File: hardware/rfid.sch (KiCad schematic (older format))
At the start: 29 parts

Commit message: Annotated schematic, generated netlist, and assigned footprints to all of the passives. Only connectors, IC, and crystal footprints have to be made and assigned.
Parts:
- gave numbers to parts that had none: 29
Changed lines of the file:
@@
 $EndDescr
 $Comp
-L CR95HF U?
+L CR95HF U1
 U 1 1 541504F3
 P 3525 2245
-F 0 "U?" H 3990 3230 39  0000 C CNN
+F 0 "U1" H 3990 3230 39  0000 C CNN
 F 1 "CR95HF" H 3015 3230 39  0000 C CNN
 F 2 "" H 3485 2765 20  0000 C CNN
@@
 $EndComp
 $Comp
-L MURATA_CRYSTAL_SMD X?
+L MURATA_CRYSTAL_SMD X1
 U 1 1 54173929
 P 2365 2700
-F 0 "X?" V 2255 2765 30  0000 C CNN
+F 0 "X1" V 2255 2765 30  0000 C CNN
 F 1 "27.12MHz" V 2370 2770 30  0000 L CNN
 F 2 "" H 2365 2700 60  0000 C CNN
@@
 $EndComp
 $Comp
-L capacitor C?
+L capacitor C1
 U 1 1 54173C81
 P 2020 2530
-F 0 "C?" V 1980 2585 40  0000 L CNN
+F 0 "C1" V 1980 2585 40  0000 L CNN
 F 1 "4pF" V 1970 2370 40  0000 L CNN
 F 2 "" H 2058 2380 30  0000 C CNN
@@
 $EndComp
 $Comp
-L capacitor C?
+L capacitor C2
 U 1 1 54173DFA
 P 2020 2870
-F 0 "C?" V 1975 2920 40  0000 L CNN
+F 0 "C2" V 1975 2920 40  0000 L CNN
 F 1 "4pF" V 1965 2710 40  0000 L CNN
 F 2 "" H 2058 2720 30  0000 C CNN
@@
 Connection ~ 2365 2870
 $Comp
-L GND #PWR?
+L GND #PWR01
 U 1 1 54173FD6
 P 1670 2730
-F 0 "#PWR?" H 1670 2730 30  0001 C CNN
+F 0 "#PWR01" H 1670 2730 30  0001 C CNN
 F 1 "GND" H 1670 2660 30  0001 C CNN
 F 2 "" H 1670 2730 60  0000 C CNN
@@
 Connection ~ 1800 2660
 $Comp
-L capacitor C?
+L capacitor C7
 U 1 1 54175E86
 P 2690 3385
-F 0 "C?" H 2710 3460 40  0000 L CNN
+F 0 "C7" H 2710 3460 40  0000 L CNN
 F 1 "1nF" H 2710 3305 40  0000 L CNN
 F 2 "" H 2728 3235 30  0000 C CNN
@@
 	2690 3180 2690 3275
 $Comp
-L GND #PWR?
+L GND #PWR02
 U 1 1 54175FA9
 P 2690 3545
-F 0 "#PWR?" H 2690 3545 30  0001 C CNN
+F 0 "#PWR02" H 2690 3545 30  0001 C CNN
 F 1 "GND" H 2690 3475 30  0001 C CNN
 F 2 "" H 2690 3545 60  0000 C CNN
@@
 3V3
 $Comp
-L resistor R?
+L resistor R4
 U 1 1 54191892
 P 2635 1310
-F 0 "R?" H 2550 1360 40  0000 C CNN
+F 0 "R4" H 2550 1360 40  0000 C CNN
 F 1 "3.3k" H 2560 1440 40  0000 C CNN
 F 2 "" V 2565 1310 30  0000 C CNN
@@
 Connection ~ 3495 1100
 $Comp
-L GND #PWR?
+L GND #PWR03
 U 1 1 54191BE5
 P 2680 2355
-F 0 "#PWR?" H 2680 2355 30  0001 C CNN
+F 0 "#PWR03" H 2680 2355 30  0001 C CNN
 F 1 "GND" H 2680 2285 30  0001 C CNN
 F 2 "" H 2680 2355 60  0000 C CNN
@@
 	2205 2065 2785 2065
 $Comp
-L CONN_01X06 P?
+L CONN_01X06 P2
 U 1 1 54192185
 P 2005 1815
-F 0 "P?" H 2005 1465 50  0000 C CNN
+F 0 "P2" H 2005 1465 50  0000 C CNN
 F 1 "COMMS" V 2105 1815 50  0000 C CNN
 F 2 "" H 2005 1815 60  0000 C CNN
@@
 	2300 1565 2205 1565
 $Comp
-L resistor R?
+L resistor R1
 U 1 1 541A2E55
 P 2425 1310
-F 0 "R?" H 2330 1360 40  0000 C CNN
+F 0 "R1" H 2330 1360 40  0000 C CNN
 F 1 "3.3k" H 2355 1440 40  0000 C CNN
 F 2 "" V 2355 1310 30  0000 C CNN
@@
 Connection ~ 2635 1100
 $Comp
-L resistor R?
+L resistor R2
 U 1 1 541A325E
 P 2450 2210
-F 0 "R?" V 2375 2285 40  0000 C CNN
+F 0 "R2" V 2375 2285 40  0000 C CNN
 F 1 "3.3k" V 2375 2135 40  0000 C CNN
 F 2 "" V 2380 2210 30  0000 C CNN
@@
 	2235 2210 2270 2210
 $Comp
-L resistor R?
+L resistor R3
 U 1 1 541A35D8
 P 2460 3100
-F 0 "R?" V 2375 3165 40  0000 C CNN
+F 0 "R3" V 2375 3165 40  0000 C CNN
 F 1 "3.3k" V 2375 3020 40  0000 C CNN
 F 2 "" V 2390 3100 30  0000 C CNN
@@
 	2185 3100 2280 3100
 $Comp
-L GND #PWR?
+L GND #PWR04
 U 1 1 541A40A6
 P 3525 3530
-F 0 "#PWR?" H 3525 3530 30  0001 C CNN
+F 0 "#PWR04" H 3525 3530 30  0001 C CNN
 F 1 "GND" H 3525 3460 30  0001 C CNN
 F 2 "" H 3525 3530 60  0000 C CNN
@@
 Connection ~ 3525 3475
 $Comp
-L CONN_01X02 P?
+L CONN_01X02 P1
 U 1 1 541A49C8
 P 1775 4235
-F 0 "P?" H 1775 4385 50  0000 C CNN
+F 0 "P1" H 1775 4385 50  0000 C CNN
 F 1 "CONN_01X02" V 1875 4235 50  0000 C CNN
 F 2 "" H 1775 4235 60  0000 C CNN
@@
 	3580 1175 3580 1050
 $Comp
-L GND #PWR?
+L GND #PWR05
 U 1 1 541A5357
 P 2030 4335
-F 0 "#PWR?" H 2030 4335 30  0001 C CNN
+F 0 "#PWR05" H 2030 4335 30  0001 C CNN
 F 1 "GND" H 2030 4265 30  0001 C CNN
 F 2 "" H 2030 4335 60  0000 C CNN
@@
 3V3_RF
 $Comp
-L INDUCTOR_SMALL L?
+L INDUCTOR_SMALL L1
 U 1 1 541A56A3
 P 2190 4515
-F 0 "L?" H 2190 4615 50  0000 C CNN
+F 0 "L1" H 2190 4615 50  0000 C CNN
 F 1 "tx_3v3_choke" H 2190 4465 50  0000 C CNN
 F 2 "" H 2190 4515 60  0000 C CNN
@@
 $EndComp
 $Comp
-L capacitor C?
+L capacitor C3
 U 1 1 541A58CF
 P 2425 4370
-F 0 "C?" H 2445 4445 40  0000 L CNN
+F 0 "C3" H 2445 4445 40  0000 L CNN
 F 1 "10nF" H 2440 4285 40  0000 L CNN
 F 2 "" H 2463 4220 30  0000 C CNN
@@
 $EndComp
 $Comp
-L capacitor C?
+L capacitor C5
 U 1 1 541A5A22
 P 2685 4370
-F 0 "C?" H 2705 4445 40  0000 L CNN
+F 0 "C5" H 2705 4445 40  0000 L CNN
 F 1 "100nF" H 2705 4280 40  0000 L CNN
 F 2 "" H 2723 4220 30  0000 C CNN
@@
 $EndComp
 $Comp
-L Polarized_Capacitor C?
+L Polarized_Capacitor C8
 U 1 1 541A5A83
 P 2965 4365
-F 0 "C?" H 2990 4440 39  0000 L CNN
+F 0 "C8" H 2990 4440 39  0000 L CNN
 F 1 "1uF" H 3015 4270 39  0000 L CNN
 F 2 "" H 2965 4365 60  0000 C CNN
@@
 $EndComp
 $Comp
-L Polarized_Capacitor C?
+L Polarized_Capacitor C9
 U 1 1 541A5D75
 P 2965 5005
-F 0 "C?" H 2990 5080 50  0000 L CNN
+F 0 "C9" H 2990 5080 50  0000 L CNN
 F 1 "4.7uF" H 3000 4910 39  0000 L CNN
 F 2 "" H 2965 5005 60  0000 C CNN
@@
 $EndComp
 $Comp
-L capacitor C?
+L capacitor C6
 U 1 1 541A5E22
 P 2685 5010
-F 0 "C?" H 2705 5085 40  0000 L CNN
+F 0 "C6" H 2705 5085 40  0000 L CNN
 F 1 "100nF" H 2700 4920 40  0000 L CNN
 F 2 "" H 2723 4860 30  0000 C CNN
@@
 $EndComp
 $Comp
-L capacitor C?
+L capacitor C4
 U 1 1 541A5EC3
 P 2425 5015
-F 0 "C?" H 2445 5090 40  0000 L CNN
+F 0 "C4" H 2445 5090 40  0000 L CNN
 F 1 "10nF" H 2445 4935 40  0000 L CNN
 F 2 "" H 2463 4865 30  0000 C CNN
@@
 Connection ~ 2965 4845
 $Comp
-L GND #PWR?
+L GND #PWR06
 U 1 1 541A734A
 P 2585 4585
-F 0 "#PWR?" H 2585 4585 30  0001 C CNN
+F 0 "#PWR06" H 2585 4585 30  0001 C CNN
 F 1 "GND" H 2585 4515 30  0001 C CNN
 F 2 "" H 2585 4585 60  0000 C CNN
@@
 $EndComp
 $Comp
-L GND #PWR?
+L GND #PWR07
 U 1 1 541A750E
 P 2585 5215
-F 0 "#PWR?" H 2585 5215 30  0001 C CNN
+F 0 "#PWR07" H 2585 5215 30  0001 C CNN
 F 1 "GND" H 2585 5145 30  0001 C CNN
 F 2 "" H 2585 5215 60  0000 C CNN
@@
 Connection ~ 2585 5165
 $Comp
-L capacitor C?
+L capacitor C10
 U 1 1 541FBF59
 P 4935 1520
-F 0 "C?" V 4985 1550 40  0000 L CNN
+F 0 "C10" V 4985 1550 40  0000 L CNN
 F 1 "open" V 4980 1335 40  0000 L CNN
 F 2 "" H 4973 1370 30  0000 C CNN
@@
 $EndComp
 $Comp
-L capacitor C?
+L capacitor C11
 U 1 1 541FC0D8
 P 4935 1720
-F 0 "C?" V 4895 1750 40  0000 L CNN
+F 0 "C11" V 4895 1750 40  0000 L CNN
 F 1 "open" V 4895 1535 40  0000 L CNN
 F 2 "" H 4973 1570 30  0000 C CNN
@@
 $EndComp
 $Comp
-L capacitor C?
+L capacitor C12
 U 1 1 541FC26B
 P 5490 1475
-F 0 "C?" V 5555 1525 40  0000 L CNN
+F 0 "C12" V 5555 1525 40  0000 L CNN
 F 1 "150pF" V 5555 1245 40  0000 L CNN
 F 2 "" H 5528 1325 30  0000 C CNN
@@
 $EndComp
 $Comp
-L capacitor C?
+L capacitor C13
 U 1 1 541FC326
 P 5490 1775
-F 0 "C?" V 5550 1825 40  0000 L CNN
+F 0 "C13" V 5550 1825 40  0000 L CNN
 F 1 "150pF" V 5550 1550 40  0000 L CNN
 F 2 "" H 5528 1625 30  0000 C CNN
@@
 $EndComp
 $Comp
-L capacitor C?
+L capacitor C14
 U 1 1 541FC46F
 P 5790 1620
-F 0 "C?" H 5810 1695 40  0000 L CNN
+F 0 "C14" H 5810 1695 40  0000 L CNN
 F 1 "220pF" H 5820 1555 40  0000 L CNN
 F 2 "" H 5828 1470 30  0000 C CNN
@@
 $EndComp
 $Comp
-L capacitor C?
+L capacitor C15
 U 1 1 541FC5B5
 P 6140 1620
-F 0 "C?" H 6160 1695 40  0000 L CNN
+F 0 "C15" H 6160 1695 40  0000 L CNN
 F 1 "15pF" H 6170 1555 40  0000 L CNN
 F 2 "" H 6178 1470 30  0000 C CNN
@@
 $EndComp
 $Comp
-L GND #PWR?
+L GND #PWR08
 U 1 1 541FD180
 P 5180 1655
-F 0 "#PWR?" H 5180 1655 30  0001 C CNN
+F 0 "#PWR08" H 5180 1655 30  0001 C CNN
 F 1 "GND" H 5180 1585 30  0001 C CNN
 F 2 "" H 5180 1655 60  0000 C CNN
@@
 $EndComp
 $Comp
-L resistor R?
+L resistor R7
 U 1 1 541FD7DD
 P 4495 1205
-F 0 "R?" V 4575 1205 40  0000 C CNN
+F 0 "R7" V 4575 1205 40  0000 C CNN
 F 1 "330" V 4405 1210 40  0000 C CNN
 F 2 "" V 4425 1205 30  0000 C CNN
@@
 $EndComp
 $Comp
-L resistor R?
+L resistor R8
 U 1 1 541FDA06
 P 4495 1475
-F 0 "R?" V 4575 1475 40  0000 C CNN
+F 0 "R8" V 4575 1475 40  0000 C CNN
 F 1 "0" V 4405 1480 40  0000 C CNN
 F 2 "" V 4425 1475 30  0000 C CNN
@@
 $EndComp
 $Comp
-L resistor R?
+L resistor R5
 U 1 1 541FDC12
 P 4485 1775
-F 0 "R?" V 4565 1775 40  0000 C CNN
+F 0 "R5" V 4565 1775 40  0000 C CNN
 F 1 "0" V 4395 1780 40  0000 C CNN
 F 2 "" V 4415 1775 30  0000 C CNN
@@
 $EndComp
 $Comp
-L resistor R?
+L resistor R6
 U 1 1 541FDD23
 P 4485 2055
-F 0 "R?" V 4565 2055 40  0000 C CNN
+F 0 "R6" V 4565 2055 40  0000 C CNN
 F 1 "330" V 4395 2060 40  0000 C CNN
 F 2 "" V 4415 2055 30  0000 C CNN
@@
 	4235 1775 4305 1775
 $Comp
-L resistor R?
+L resistor R9
 U 1 1 542007D4
 P 6490 1620
-F 0 "R?" H 6595 1655 40  0000 C CNN
+F 0 "R9" H 6595 1655 40  0000 C CNN
 F 1 "2.26k" H 6635 1575 40  0000 C CNN
 F 2 "" V 6420 1620 30  0000 C CNN

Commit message: CR95HF schematic symbol had the belly pad labeled as ~. Changed to 33 and updated schematic, netlist, library, etc.
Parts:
- C1, C10, C11, C12, C13, C14, C15, C2, C3, C4, C5, C6, C7, C8, L1, R1, R2, R3, R4, R5, R6, R7, R8, R9: footprint (none) -> SMD_Packages:SMD-0603
- C9: footprint (none) -> SMD_Packages:SMD-0805
- P1: footprint (none) -> rfid:JST_PH_2pin_side
- P2: footprint (none) -> rfid:JST_PH_6pin
- U1: footprint (none) -> SMD_Packages:QFN-32-1EP
- X1: footprint (none) -> rfid:2x1.6_crystal
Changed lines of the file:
@@
 LIBS:valves
 LIBS:rfid
+LIBS:rfid-cache
 EELAYER 24 0
 EELAYER END
@@
 F 0 "U1" H 3990 3230 39  0000 C CNN
 F 1 "CR95HF" H 3015 3230 39  0000 C CNN
-F 2 "" H 3485 2765 20  0000 C CNN
+F 2 "SMD_Packages:QFN-32-1EP" H 3485 2765 20  0001 C CNN
 F 3 "" H 3485 2765 20  0000 C CNN
 	1    3525 2245
@@
 F 0 "X1" V 2255 2765 30  0000 C CNN
 F 1 "27.12MHz" V 2370 2770 30  0000 L CNN
-F 2 "" H 2365 2700 60  0000 C CNN
+F 2 "rfid:2x1.6_crystal" H 2365 2700 60  0001 C CNN
 F 3 "" H 2365 2700 60  0000 C CNN
 	1    2365 2700
@@
 F 0 "C1" V 1980 2585 40  0000 L CNN
 F 1 "4pF" V 1970 2370 40  0000 L CNN
-F 2 "" H 2058 2380 30  0000 C CNN
+F 2 "SMD_Packages:SMD-0603" H 2058 2380 30  0001 C CNN
 F 3 "" H 2020 2530 60  0000 C CNN
 	1    2020 2530
@@
 F 0 "C2" V 1975 2920 40  0000 L CNN
 F 1 "4pF" V 1965 2710 40  0000 L CNN
-F 2 "" H 2058 2720 30  0000 C CNN
+F 2 "SMD_Packages:SMD-0603" H 2058 2720 30  0001 C CNN
 F 3 "" H 2020 2870 60  0000 C CNN
 	1    2020 2870
@@
 F 0 "C7" H 2710 3460 40  0000 L CNN
 F 1 "1nF" H 2710 3305 40  0000 L CNN
-F 2 "" H 2728 3235 30  0000 C CNN
+F 2 "SMD_Packages:SMD-0603" H 2728 3235 30  0001 C CNN
 F 3 "" H 2690 3385 60  0000 C CNN
 	1    2690 3385
@@
 F 0 "R4" H 2550 1360 40  0000 C CNN
 F 1 "3.3k" H 2560 1440 40  0000 C CNN
-F 2 "" V 2565 1310 30  0000 C CNN
+F 2 "SMD_Packages:SMD-0603" V 2565 1310 30  0001 C CNN
 F 3 "" H 2635 1310 30  0000 C CNN
 	1    2635 1310
@@
 F 0 "P2" H 2005 1465 50  0000 C CNN
 F 1 "COMMS" V 2105 1815 50  0000 C CNN
-F 2 "" H 2005 1815 60  0000 C CNN
+F 2 "rfid:JST_PH_6pin" H 2005 1815 60  0001 C CNN
 F 3 "" H 2005 1815 60  0000 C CNN
 	1    2005 1815
@@
 F 0 "R1" H 2330 1360 40  0000 C CNN
 F 1 "3.3k" H 2355 1440 40  0000 C CNN
-F 2 "" V 2355 1310 30  0000 C CNN
+F 2 "SMD_Packages:SMD-0603" V 2355 1310 30  0001 C CNN
 F 3 "" H 2425 1310 30  0000 C CNN
 	1    2425 1310
@@
 F 0 "R2" V 2375 2285 40  0000 C CNN
 F 1 "3.3k" V 2375 2135 40  0000 C CNN
-F 2 "" V 2380 2210 30  0000 C CNN
+F 2 "SMD_Packages:SMD-0603" V 2380 2210 30  0001 C CNN
 F 3 "" H 2450 2210 30  0000 C CNN
 	1    2450 2210
@@
 F 0 "R3" V 2375 3165 40  0000 C CNN
 F 1 "3.3k" V 2375 3020 40  0000 C CNN
-F 2 "" V 2390 3100 30  0000 C CNN
+F 2 "SMD_Packages:SMD-0603" V 2390 3100 30  0001 C CNN
 F 3 "" H 2460 3100 30  0000 C CNN
 	1    2460 3100
@@
 F 0 "P1" H 1775 4385 50  0000 C CNN
 F 1 "CONN_01X02" V 1875 4235 50  0000 C CNN
-F 2 "" H 1775 4235 60  0000 C CNN
+F 2 "rfid:JST_PH_2pin_side" H 1775 4235 60  0001 C CNN
 F 3 "" H 1775 4235 60  0000 C CNN
 	1    1775 4235
@@
 F 0 "L1" H 2190 4615 50  0000 C CNN
 F 1 "tx_3v3_choke" H 2190 4465 50  0000 C CNN
-F 2 "" H 2190 4515 60  0000 C CNN
+F 2 "SMD_Packages:SMD-0603" H 2190 4515 60  0001 C CNN
 F 3 "" H 2190 4515 60  0000 C CNN
 	1    2190 4515
@@
 F 0 "C3" H 2445 4445 40  0000 L CNN
 F 1 "10nF" H 2440 4285 40  0000 L CNN
-F 2 "" H 2463 4220 30  0000 C CNN
+F 2 "SMD_Packages:SMD-0603" H 2463 4220 30  0001 C CNN
 F 3 "" H 2425 4370 60  0000 C CNN
 	1    2425 4370
@@
 F 0 "C5" H 2705 4445 40  0000 L CNN
 F 1 "100nF" H 2705 4280 40  0000 L CNN
-F 2 "" H 2723 4220 30  0000 C CNN
+F 2 "SMD_Packages:SMD-0603" H 2723 4220 30  0001 C CNN
 F 3 "" H 2685 4370 60  0000 C CNN
 	1    2685 4370
@@
 F 0 "C8" H 2990 4440 39  0000 L CNN
 F 1 "1uF" H 3015 4270 39  0000 L CNN
-F 2 "" H 2965 4365 60  0000 C CNN
+F 2 "SMD_Packages:SMD-0603" H 2965 4365 60  0001 C CNN
 F 3 "" H 2965 4365 60  0000 C CNN
 	1    2965 4365
@@
 F 0 "C9" H 2990 5080 50  0000 L CNN
 F 1 "4.7uF" H 3000 4910 39  0000 L CNN
-F 2 "" H 2965 5005 60  0000 C CNN
+F 2 "SMD_Packages:SMD-0805" H 2965 5005 60  0001 C CNN
 F 3 "" H 2965 5005 60  0000 C CNN
 	1    2965 5005
@@
 F 0 "C6" H 2705 5085 40  0000 L CNN
 F 1 "100nF" H 2700 4920 40  0000 L CNN
-F 2 "" H 2723 4860 30  0000 C CNN
+F 2 "SMD_Packages:SMD-0603" H 2723 4860 30  0001 C CNN
 F 3 "" H 2685 5010 60  0000 C CNN
 	1    2685 5010
@@
 F 0 "C4" H 2445 5090 40  0000 L CNN
 F 1 "10nF" H 2445 4935 40  0000 L CNN
-F 2 "" H 2463 4865 30  0000 C CNN
+F 2 "SMD_Packages:SMD-0603" H 2463 4865 30  0001 C CNN
 F 3 "" H 2425 5015 60  0000 C CNN
 	1    2425 5015
@@
 F 0 "C10" V 4985 1550 40  0000 L CNN
 F 1 "open" V 4980 1335 40  0000 L CNN
-F 2 "" H 4973 1370 30  0000 C CNN
+F 2 "SMD_Packages:SMD-0603" H 4973 1370 30  0001 C CNN
 F 3 "" H 4935 1520 60  0000 C CNN
 	1    4935 1520
@@
 F 0 "C11" V 4895 1750 40  0000 L CNN
 F 1 "open" V 4895 1535 40  0000 L CNN
-F 2 "" H 4973 1570 30  0000 C CNN
+F 2 "SMD_Packages:SMD-0603" H 4973 1570 30  0001 C CNN
 F 3 "" H 4935 1720 60  0000 C CNN
 	1    4935 1720
@@
 F 0 "C12" V 5555 1525 40  0000 L CNN
 F 1 "150pF" V 5555 1245 40  0000 L CNN
-F 2 "" H 5528 1325 30  0000 C CNN
+F 2 "SMD_Packages:SMD-0603" H 5528 1325 30  0001 C CNN
 F 3 "" H 5490 1475 60  0000 C CNN
 	1    5490 1475
@@
 F 0 "C13" V 5550 1825 40  0000 L CNN
 F 1 "150pF" V 5550 1550 40  0000 L CNN
-F 2 "" H 5528 1625 30  0000 C CNN
+F 2 "SMD_Packages:SMD-0603" H 5528 1625 30  0001 C CNN
 F 3 "" H 5490 1775 60  0000 C CNN
 	1    5490 1775
@@
 F 0 "C14" H 5810 1695 40  0000 L CNN
 F 1 "220pF" H 5820 1555 40  0000 L CNN
-F 2 "" H 5828 1470 30  0000 C CNN
+F 2 "SMD_Packages:SMD-0603" H 5828 1470 30  0001 C CNN
 F 3 "" H 5790 1620 60  0000 C CNN
 	1    5790 1620
@@
 F 0 "C15" H 6160 1695 40  0000 L CNN
 F 1 "15pF" H 6170 1555 40  0000 L CNN
-F 2 "" H 6178 1470 30  0000 C CNN
+F 2 "SMD_Packages:SMD-0603" H 6178 1470 30  0001 C CNN
 F 3 "" H 6140 1620 60  0000 C CNN
 	1    6140 1620
@@
 F 0 "R7" V 4575 1205 40  0000 C CNN
 F 1 "330" V 4405 1210 40  0000 C CNN
-F 2 "" V 4425 1205 30  0000 C CNN
+F 2 "SMD_Packages:SMD-0603" V 4425 1205 30  0001 C CNN
 F 3 "" H 4495 1205 30  0000 C CNN
 	1    4495 1205
@@
 F 0 "R8" V 4575 1475 40  0000 C CNN
 F 1 "0" V 4405 1480 40  0000 C CNN
-F 2 "" V 4425 1475 30  0000 C CNN
+F 2 "SMD_Packages:SMD-0603" V 4425 1475 30  0001 C CNN
 F 3 "" H 4495 1475 30  0000 C CNN
 	1    4495 1475
@@
 F 0 "R5" V 4565 1775 40  0000 C CNN
 F 1 "0" V 4395 1780 40  0000 C CNN
-F 2 "" V 4415 1775 30  0000 C CNN
+F 2 "SMD_Packages:SMD-0603" V 4415 1775 30  0001 C CNN
 F 3 "" H 4485 1775 30  0000 C CNN
 	1    4485 1775
@@
 F 0 "R6" V 4565 2055 40  0000 C CNN
 F 1 "330" V 4395 2060 40  0000 C CNN
-F 2 "" V 4415 2055 30  0000 C CNN
+F 2 "SMD_Packages:SMD-0603" V 4415 2055 30  0001 C CNN
 F 3 "" H 4485 2055 30  0000 C CNN
 	1    4485 2055
@@
 F 0 "R9" H 6595 1655 40  0000 C CNN
 F 1 "2.26k" H 6635 1575 40  0000 C CNN
-F 2 "" V 6420 1620 30  0000 C CNN
+F 2 "SMD_Packages:SMD-0603" V 6420 1620 30  0001 C CNN
 F 3 "" H 6490 1620 30  0000 C CNN
 	1    6490 1620

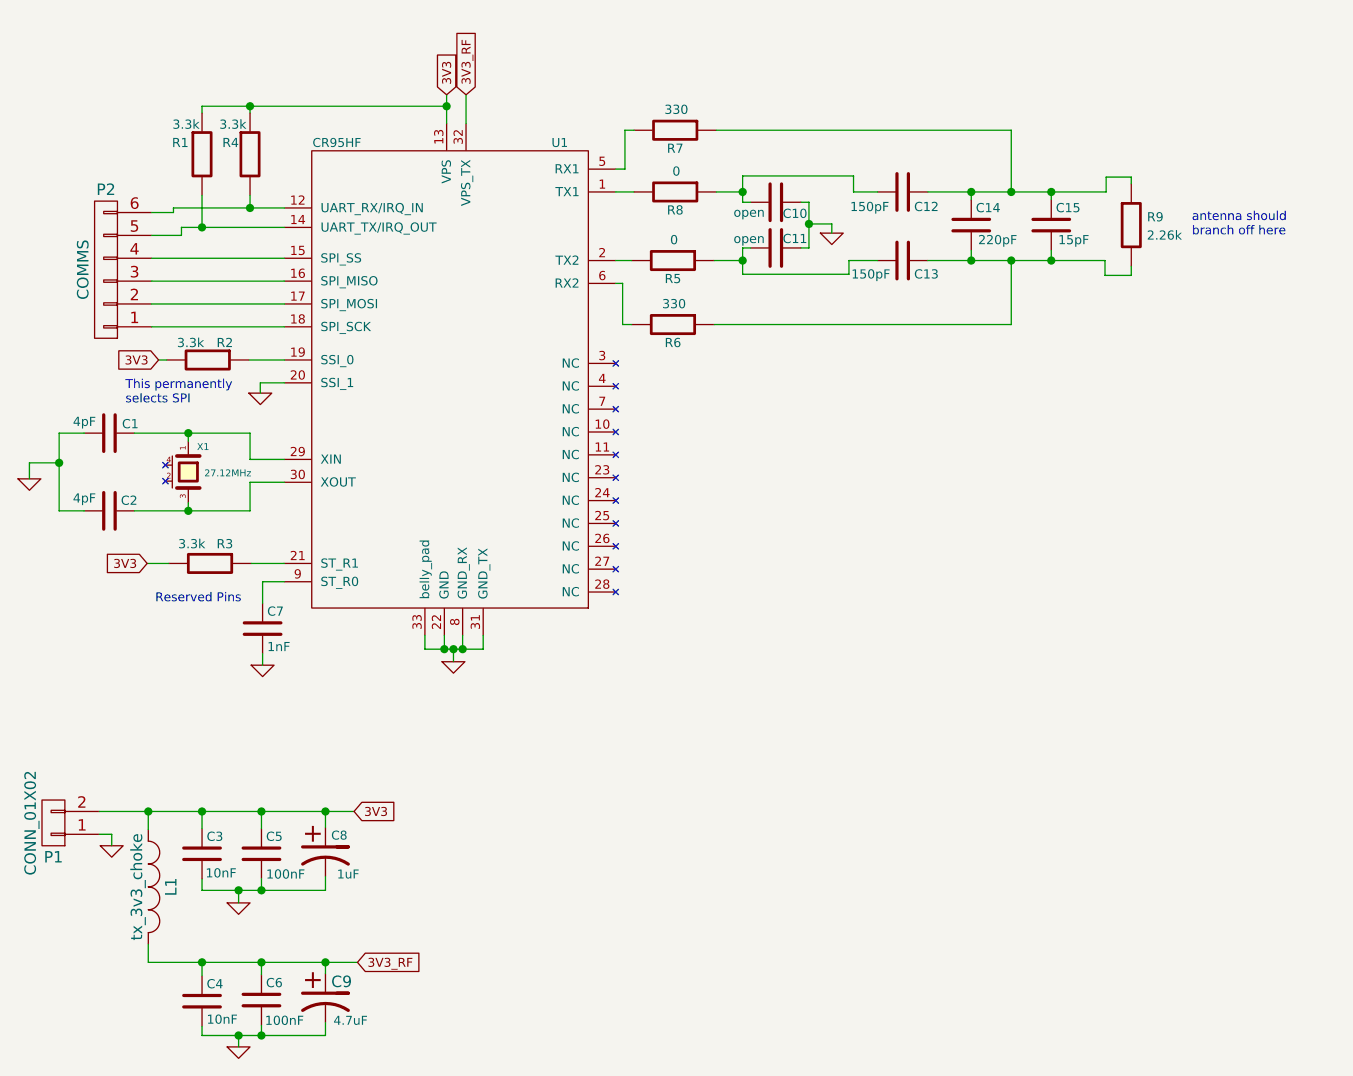
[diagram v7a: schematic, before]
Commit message: Shorted resistor attached to antenna in schematic like the antenna basically will (to prevent DRC errors). Also renamed the crystal from X1 to G1.
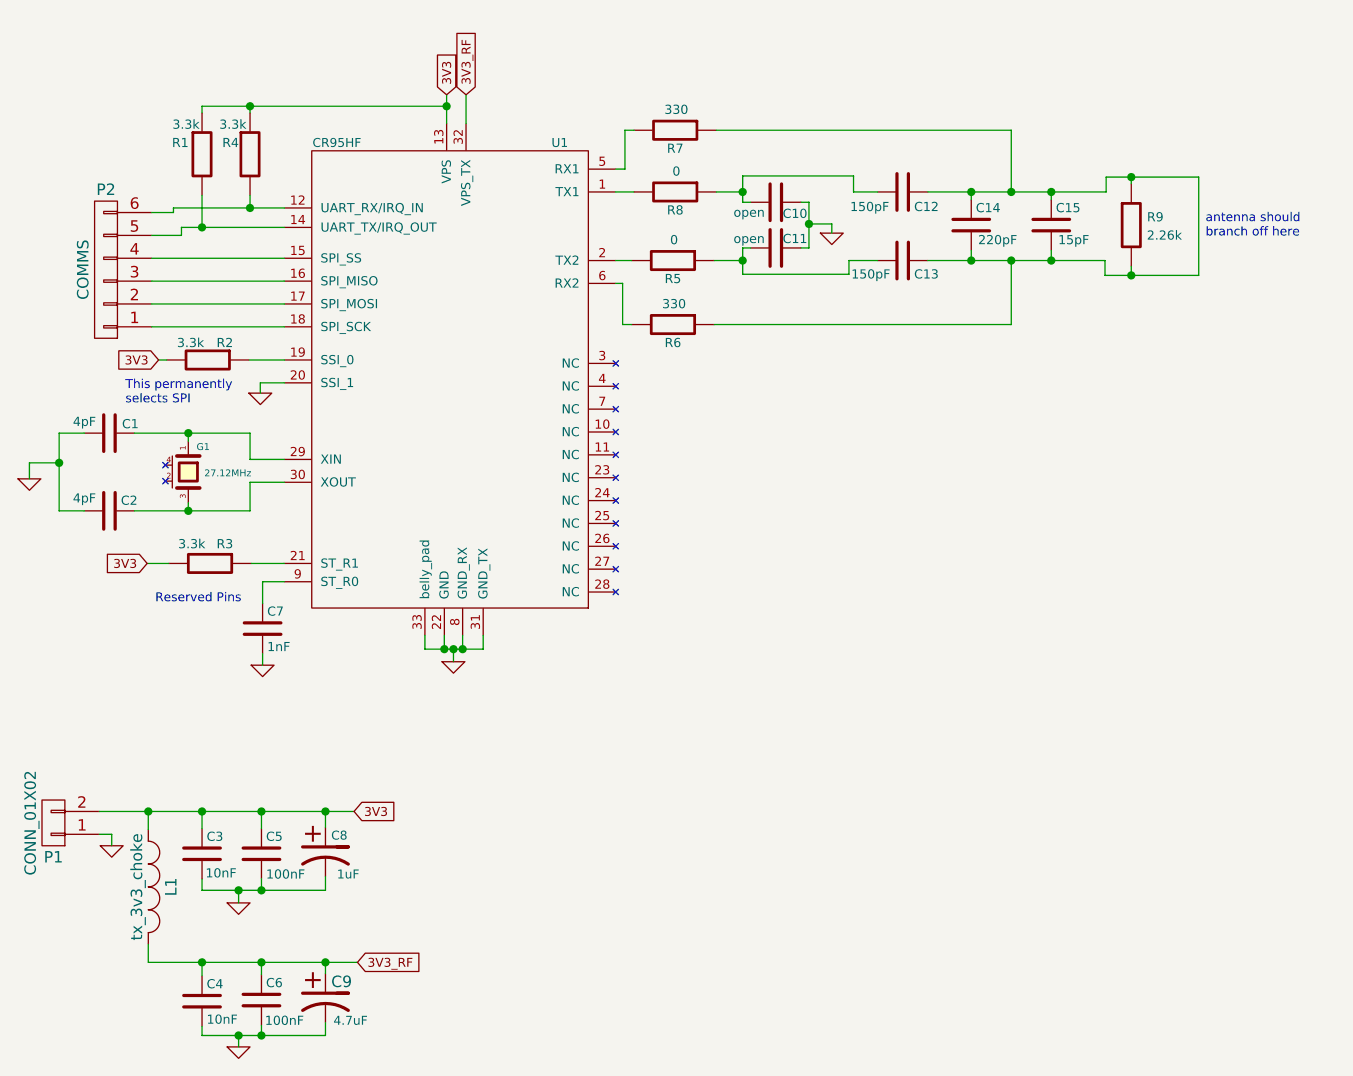
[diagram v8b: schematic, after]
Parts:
- renumbered X1 to G1
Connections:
- net at C12.1, C14.1, C15.1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: now also C13.1, C14.2, C15.2, R6.1, R9.2
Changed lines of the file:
@@
 $EndComp
 $Comp
-L MURATA_CRYSTAL_SMD X1
+L MURATA_CRYSTAL_SMD G1
 U 1 1 54173929
 P 2365 2700
-F 0 "X1" V 2255 2765 30  0000 C CNN
+F 0 "G1" V 2255 2765 30  0000 C CNN
 F 1 "27.12MHz" V 2370 2770 30  0000 L CNN
 F 2 "rfid:2x1.6_crystal" H 2365 2700 60  0001 C CNN
@@
 	6380 1475 6380 1410
 Wire Wire Line
-	6380 1410 6490 1410
+	6380 1410 6785 1410
 Wire Wire Line
 	6490 1410 6490 1440
@@
 	6375 1775 6375 1840
 Wire Wire Line
-	6375 1840 6490 1840
+	6375 1840 6785 1840
 Wire Wire Line
 	6490 1840 6490 1800
@@
 	5965 1205 5965 1475
 Connection ~ 5965 1475
-Text Notes 6755 1675 0    39   ~ 0
+Text Notes 6815 1680 0    39   ~ 0
 antenna should \nbranch off here
+Wire Wire Line
+	6785 1840 6785 1410
+Connection ~ 6490 1840
+Connection ~ 6490 1410
 $EndSCHEMATC
